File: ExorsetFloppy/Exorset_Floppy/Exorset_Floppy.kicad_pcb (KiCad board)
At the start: 2 copper layers, 160 x 100 mm, 76 parts, among them J1 BUS, J2 Floppy, J3 Conn_01x01, J4 Conn_01x01, J5 Conn_01x01, J6 Conn_01x01, Q1 BC337, U1 GAL22V10, U10 GAL22V10, U11 74HCT74, U12 74HCT74, U121 74LS624, U13 74LS91, U14 74HCT74, U15 74HCT04, U16 74HCT74, U17 74HCT00, U18 74HCT74, U19 74LS76, U2 74HCT74, U20 68B21, U21 MC4024, U22 74LS157, U221 74LS627, U23 74LS123, U24 74HC164, U27 MC4044, U28 74F163, U29 74F163, U3 74HC245, U34 6852_DIL24, U4 MC8506, U5 74F163, U6 27C32, U7 74LS240, U8 74LS244, U9 NE555P

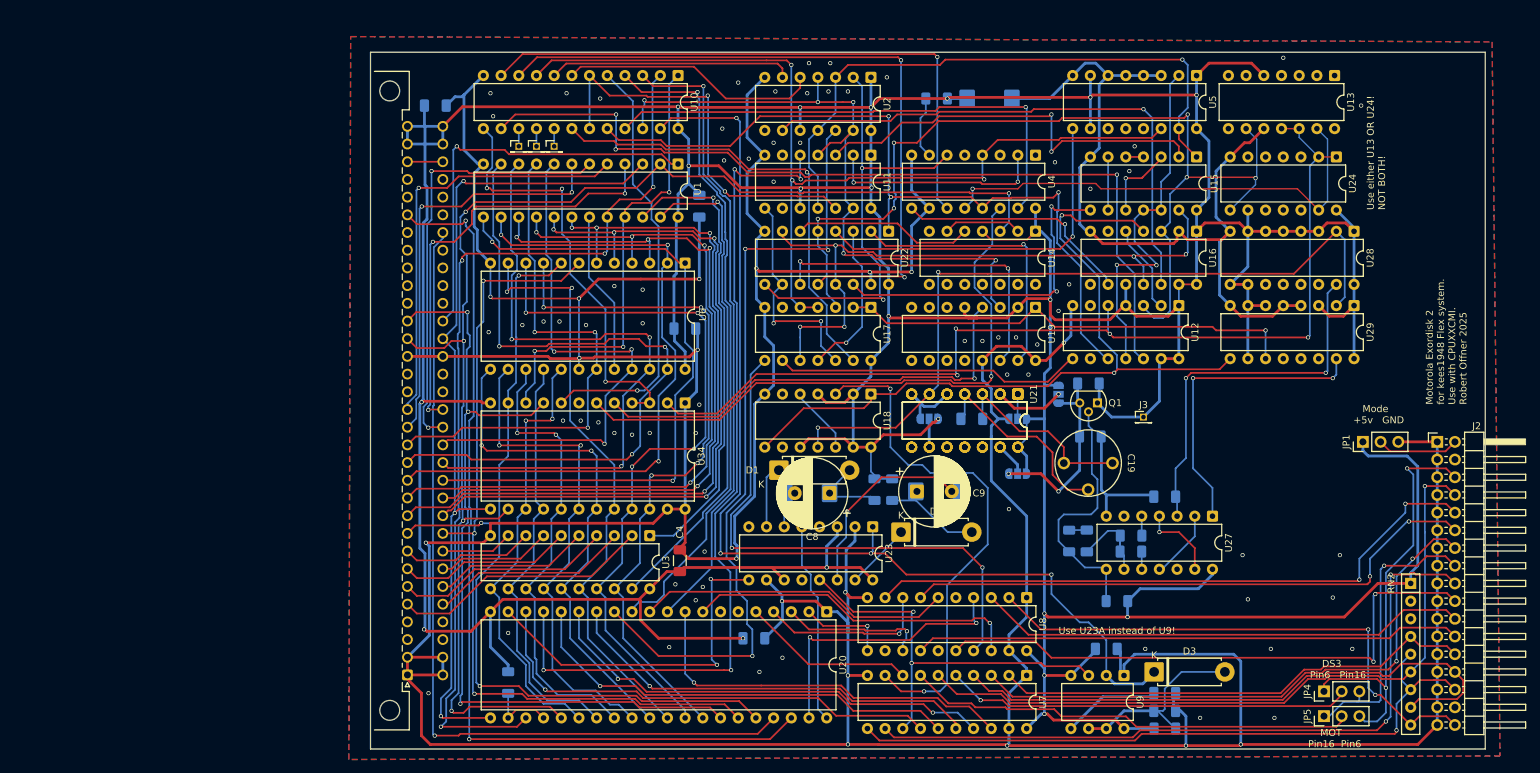
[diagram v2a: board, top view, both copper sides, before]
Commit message: Board finished, GALS added
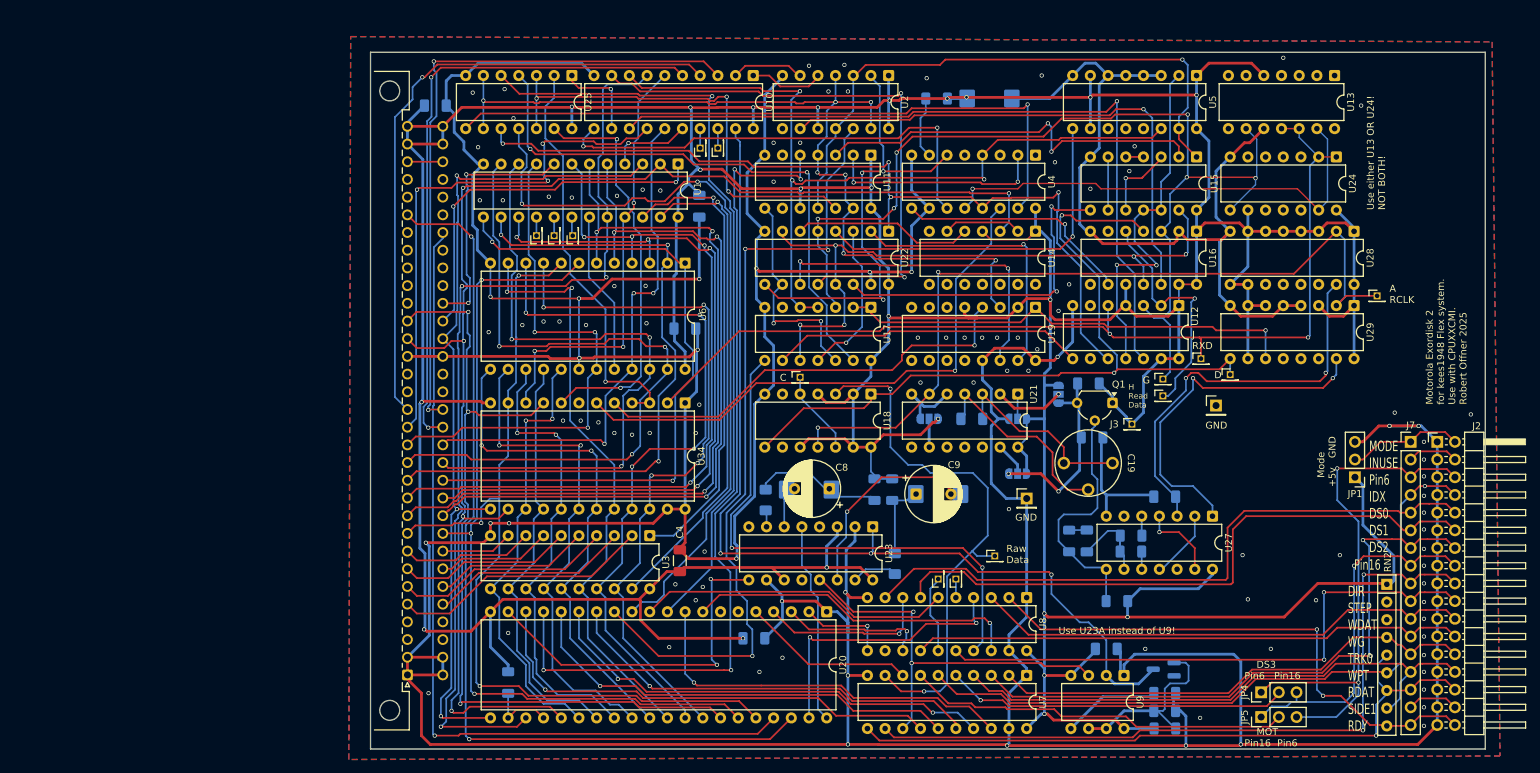
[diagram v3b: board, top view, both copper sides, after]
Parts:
- removed U121: 74LS624, Package_DIP:DIP-14_W7.62mm
- removed U221: 74LS627, Package_DIP:DIP-14_W7.62mm
- added J10: Conn_01x01, Connector_PinHeader_1.27mm:PinHeader_1x01_P1.27mm_Vertical, F.Cu at (107.3, 63.8)
- added J11: Conn_01x01, Connector_PinHeader_1.27mm:PinHeader_1x01_P1.27mm_Vertical, F.Cu at (109.9, 63.8)
- added J12: Conn_01x01, Connector_PinHeader_1.27mm:PinHeader_1x01_P1.27mm_Vertical, F.Cu at (121.7, 96.6)
- added J13: Conn_01x01, Connector_PinHeader_1.27mm:PinHeader_1x01_P1.27mm_Vertical, F.Cu at (149.6, 122.3)
- added J14: Conn_01x01, Connector_PinHeader_1.27mm:PinHeader_1x01_P1.27mm_Vertical, F.Cu at (183.4, 96.3)
- added J15: Conn_01x01, Connector_PinHeader_1.27mm:PinHeader_1x01_P1.27mm_Vertical, F.Cu at (204.5, 85.0)
- added J16: Conn_01x01, Connector_PinHeader_1.27mm:PinHeader_1x01_P1.27mm_Vertical, F.Cu at (173.7, 96.9)
- added J17: Conn_01x01, Connector_PinHeader_1.27mm:PinHeader_1x01_P1.27mm_Vertical, F.Cu at (173.7, 99.3)
- added J18: Conn_01x01, Connector_PinHeader_1.27mm:PinHeader_1x01_P1.27mm_Vertical, F.Cu at (179.2, 94.0)
- added J19: Conn_01x01, Connector_PinHeader_2.54mm:PinHeader_1x01_P2.54mm_Vertical, F.Cu at (181.4, 100.7)
- added J20: Conn_01x01, Connector_PinHeader_2.54mm:PinHeader_1x01_P2.54mm_Vertical, F.Cu at (154.2, 114.0)
- added J7: Conn_01x17, Connector_PinHeader_2.54mm:PinHeader_1x17_P2.54mm_Vertical, F.Cu at (209.3, 105.9)
- added J8: Conn_01x01, Connector_PinHeader_1.27mm:PinHeader_1x01_P1.27mm_Vertical, F.Cu at (141.5, 125.6)
- added J9: Conn_01x01, Connector_PinHeader_1.27mm:PinHeader_1x01_P1.27mm_Vertical, F.Cu at (144.0, 125.6)
- added U25: 74LS04, Package_DIP:DIP-14_W7.62mm, F.Cu at (88.9, 53.3)
- C8, C9: footprint Capacitor_THT:CP_Radial_D10.0mm_P5.00mm -> Capacitor_THT:CP_Radial_D8.0mm_P5.00mm
- D1, D2: footprint Diode_THT:D_5W_P10.16mm_Horizontal -> Diode_SMD:D_1206_3216Metric_Pad1.42x1.75mm_HandSolder; moved to B.Cu
- D3: value BAT42 -> BAS40-04; footprint Diode_THT:D_5W_P10.16mm_Horizontal -> Package_TO_SOT_SMD:SOT-23_Handsoldering; moved to B.Cu
- Q1: footprint Package_TO_SOT_THT:TO-92L -> Package_TO_SOT_THT:TO-92L_Wide
- U10: value GAL22V10 -> GAL16V8; footprint Package_DIP:DIP-24_W7.62mm -> Package_DIP:DIP-20_W7.62mm
- moved J6 15.0 mm to (89.0, 76.3), turned to 90 degrees
- moved J4 13.1 mm to (83.8, 76.3), turned to 90 degrees
- moved J5 13.1 mm to (86.4, 76.3), turned to 90 degrees
- moved U10 10.8 mm to (114.9, 53.3)
- moved JP4 9.02 mm to (187.8, 141.9)
- moved JP5 9.02 mm to (187.8, 145.4)
- moved JP1 5.21 mm to (201.3, 111.0), turned to 180 degrees
- moved D1 4.69 mm to (116.7, 114.3), turned to 90 degrees
- moved D2 4.62 mm to (135.3, 123.4), turned to 90 degrees
- moved RN2 3.43 mm to (205.9, 126.4)
- moved U2 2.55 mm to (134.4, 53.3)
- moved Q1 2.16 mm to (166.5, 100.3)
- moved J3 1.94 mm to (169.3, 103.4)
- moved D3 1.42 mm to (173.8, 138.6), turned to 180 degrees
- moved C8 0.64 mm to (125.9, 112.6)
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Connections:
- C21 pad 1: Net-(D3-A) -> Net-(U9-DIS)
- D3 pad 1: /Floppy Logic/~{RFF} -> Net-(U9-DIS)
- D3 pad 2: Net-(D3-A) -> unconnected-(D3-Pad2)
- R2 pad 1: Net-(D3-A) -> Net-(U9-DIS)
- U1 pad 16: /BA4 -> Net-(J4-Pin_1)
- U1 pad 17: /BA3 -> Net-(J5-Pin_1)
- U1 pad 18: /BA2 -> Net-(J6-Pin_1)
- U1 pad 4: /BA15 -> /SEL
- U1 pad 5: /BA14 -> /BA3
- U1 pad 6: /BA13 -> /BA2
- U1 pad 7: /BA12 -> /BA4
- U1 pad 8: /BA11 -> /B_BA
- U10 pad 1: /~{6852_CS} -> Net-(U10-I1/CLK)
- U10 pad 10: /Floppy Logic/FAST -> GND
- U10 pad 12: GND -> /Floppy Logic/~{SWCLK}
- U10 pad 13: /Floppy Logic/SWCLK -> /Floppy Logic/CRC_DATA
- U10 pad 14: /Floppy Logic/CRC_DATA -> /BA12
- U10 pad 15: Net-(J6-Pin_1) -> /BA11
- U10 pad 16: Net-(J5-Pin_1) -> /SEL
- U10 pad 17: Net-(J4-Pin_1) -> Net-(J10-Pin_1)
- U10 pad 18: /Floppy Logic/TUF# -> Net-(J11-Pin_1)
- U10 pad 19: /Floppy Logic/~{TUF} -> /Floppy Logic/~{RFF}
- U10 pad 2: /~{6820_CS} -> Net-(U10-I2)
- U10 pad 20: /Floppy Logic/WRITE/~{READ} -> +5V
- U10 pad 3: /Floppy Logic/PB0 -> /BA15
- U10 pad 4: /Floppy Logic/PB2 -> /BA14
- U10 pad 5: /Floppy Logic/TUF -> /BA13
- U10 pad 6: /Floppy Logic/~{TUF} -> /~{6852_CS}
- U10 pad 7: Net-(U10-I7) -> /~{6820_CS}
- U10 pad 8: Net-(U10-I8) -> /Floppy Logic/SLOW
- U10 pad 9: /Floppy Logic/SLOW -> /Floppy Logic/FAST
- U2 pad 5: Net-(U10-I7) -> Net-(U10-I1/CLK)
- U2 pad 6: Net-(U10-I8) -> Net-(U10-I2)
- U34 pad 3: /Floppy Logic/SWCLK -> Net-(U34-RXClk)
- U34 pad 4: /Floppy Logic/SWCLK -> Net-(U34-RXClk)
- U8 pad 15: unconnected-(U8-I2b-Pad15) -> Net-(J8-Pin_1)
- U8 pad 5: unconnected-(U8-O2b-Pad5) -> Net-(J9-Pin_1)
- U9 pad 6: Net-(D3-A) -> Net-(U9-DIS)
- U9 pad 7: Net-(D3-A) -> Net-(U9-DIS)
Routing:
- net /Floppy Logic/SWCLK: track 61.7 -> 0.00 mm, vias 3 -> 0
- net Net-(U34-RXClk): track 0.00 -> 59.1 mm, vias 0 -> 1
- net Net-(U10-I7): track 37.3 -> 0.00 mm
- net /B_BA: track 0.00 -> 35.9 mm, vias 0 -> 2
- net Net-(U10-I8): track 35.0 -> 0.00 mm
- net GND: track 904.7 -> 937.4 mm, vias 86 -> 113
- net /BA15: track 62.3 -> 94.4 mm, vias 3 -> 2
- net /Floppy Logic/RESET: track 97.4 -> 129.0 mm, vias 5 -> 7
- net /BA14: track 61.0 -> 91.4 mm
- net Net-(D3-A): track 28.8 -> 0.00 mm
- net Net-(U9-DIS): track 0.00 -> 27.5 mm
- net /BA13: track 63.1 -> 90.3 mm
- net /Floppy Logic/~{RESET}: track 73.9 -> 97.6 mm
- net Net-(J17-Pin_1): track 12.9 -> 34.6 mm, vias 0 -> 1
- net /Floppy Logic/PB0: track 90.7 -> 111.1 mm
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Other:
- board text added: "A RCLK"
- board text added: "C"
- board text added: "D"
- board text added: "DIR STEP WDAT WG TRK0 WPT RDAT SIDE1 RDY"
- board text added: "G"
- board text added: "GND"
- board text added: "H Read Data"
- board text added: "J RXD"
- board text added: "MODE INUSE Pin6 IDX DS0 DS1 DS2"
- board text added: "Pin16"
- board text added: "Raw Data"
